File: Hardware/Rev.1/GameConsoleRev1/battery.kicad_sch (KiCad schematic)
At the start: 0 parts

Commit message: Added sprites
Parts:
- added C20: 100n, Capacitor_SMD:C_0402_1005Metric, symbol Device:C
- added D1: BLUE, LED_SMD:LED_0603_1608Metric, symbol Device:LED
- added D2: AMBER, LED_SMD:LED_0603_1608Metric, symbol Device:LED
- added J14: Through Hole, Connector_PinHeader_2.54mm:PinHeader_1x02_P2.54mm_Vertical, symbol Connector:Conn_01x02_Pin
- added J5: JST, Connector_JST:JST_PH_B2B-PH-K_1x02_P2.00mm_Vertical, symbol Connector:Conn_01x02_Pin
- added J6: Pack Temp, Connector_PinHeader_2.54mm:PinHeader_1x02_P2.54mm_Vertical, symbol Connector:Conn_01x02_Pin
- added JP1, JP2, JP3, JP4, JP5: Jumper_2_Open, Jumper:SolderJumper-2_P1.3mm_Open_TrianglePad1.0x1.5mm, symbol Jumper:Jumper_2_Open
- added Q1, Q2: NMOS, Package_TO_SOT_SMD:SOT-23, symbol Transistor_FET:Q_NMOS_GSD
- added R11: 2k2, Resistor_SMD:R_0805_2012Metric, symbol Device:R
- added R12: 330R, Resistor_SMD:R_0805_2012Metric, symbol Device:R
- added R13, R14, R15, R16, R17, R19, R20: 1k, Resistor_SMD:R_0805_2012Metric, symbol Device:R
- added R18: 10k, Resistor_SMD:R_0805_2012Metric, symbol Device:R
- added R21, R22: 10k, Resistor_SMD:R_0402_1005Metric, symbol Device:R
- added R41, R42: 5M1, Resistor_SMD:R_0805_2012Metric, symbol Device:R
- added U2: BQ29700DSER, Package_SON:WSON-6_1.5x1.5mm_P0.5mm, symbol Battery_Management:BQ297xy
- added U3: BQ24073RGT, Package_DFN_QFN:VQFN-16-1EP_3x3mm_P0.5mm_EP1.6x1.6mm, symbol Battery_Management:BQ24073RGT
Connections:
- new net: JP5.1 (A), R22.1
- new net: R16.1, U3.12 (ILIM)
- new net: Q1.1 (G), R41.1, U2.3 (Dout)
- new net: R20.1, U3.4 (~{CE})
- new net: R17.1, U3.14 (TMR)
- new net: JP4.2 (B), R21.1
- new net: D2.1 (K), U3.9 (~{CHG})
- new net: D2.2 (A), R13.2
- new net: C20.1, R12.2, U2.5 (BAT)
- new net: Q2.1 (G), R42.1, U2.2 (Cout)
- new net: Q1.3 (D), Q2.3 (D)
- new net: R19.1, U3.15 (TD)
- new net: R15.1, U3.16 (ISET)
- new net: D1.1 (K), U3.7 (~{PGOOD})
- new net: D1.2 (A), R14.2
- new net: R11.1, U2.6 (V-)
- new net EN1: JP3.2 (B), JP5.2 (B), U3.6 (EN1)
- new net EN2: JP2.1 (A), JP4.1 (A), U3.5 (EN2)
- new net GND: J6.1 (Pin_1), JP1.1 (A), JP2.2 (B), JP3.1 (A), Q2.2 (S), R15.2, R16.2, R17.2, R18.2, R19.2, R20.2, R42.2, U3.17 (VSS), U3.8 (VSS)
- new net IN: U3.13 (IN)
- new net OUT: R13.1, R14.1, R21.2, R22.2, U3.10 (OUT), U3.11 (OUT)
- new net Pack+: J14.2 (Pin_2), J5.1 (Pin_1), R12.1, U3.2 (BAT), U3.3 (BAT)
- new net Pack_UP-: C20.2, J14.1 (Pin_1), J5.2 (Pin_2), JP1.2 (B), Q1.2 (S), R11.2, R41.2, U2.4 (VSS)
- new net TS: J6.2 (Pin_2), R18.1, U3.1 (TS)
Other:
- note added: "10k NTC Thermister"
- note added: "10k Res for no Therm"
- note added: "Set EN1 to 0 and EN2 to OUT for ILIM resisotr charge limit"

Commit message: A
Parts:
- D1: LCSC (none) -> C965804
- D2: LCSC (none) -> C165983
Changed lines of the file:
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@@
+			)
+		)
+		(property "LCSC" "C165983"
+			(at 153.67 71.12 0)
+			(effects
+				(font
+					(size 1.27 1.27)
+				)
 			)
 		)
@@
 			)
 		)
+		(property "LCSC" "C965804"
+			(at 165.1 71.12 0)
+			(effects
+				(font
+					(size 1.27 1.27)
+				)
+			)
+		)

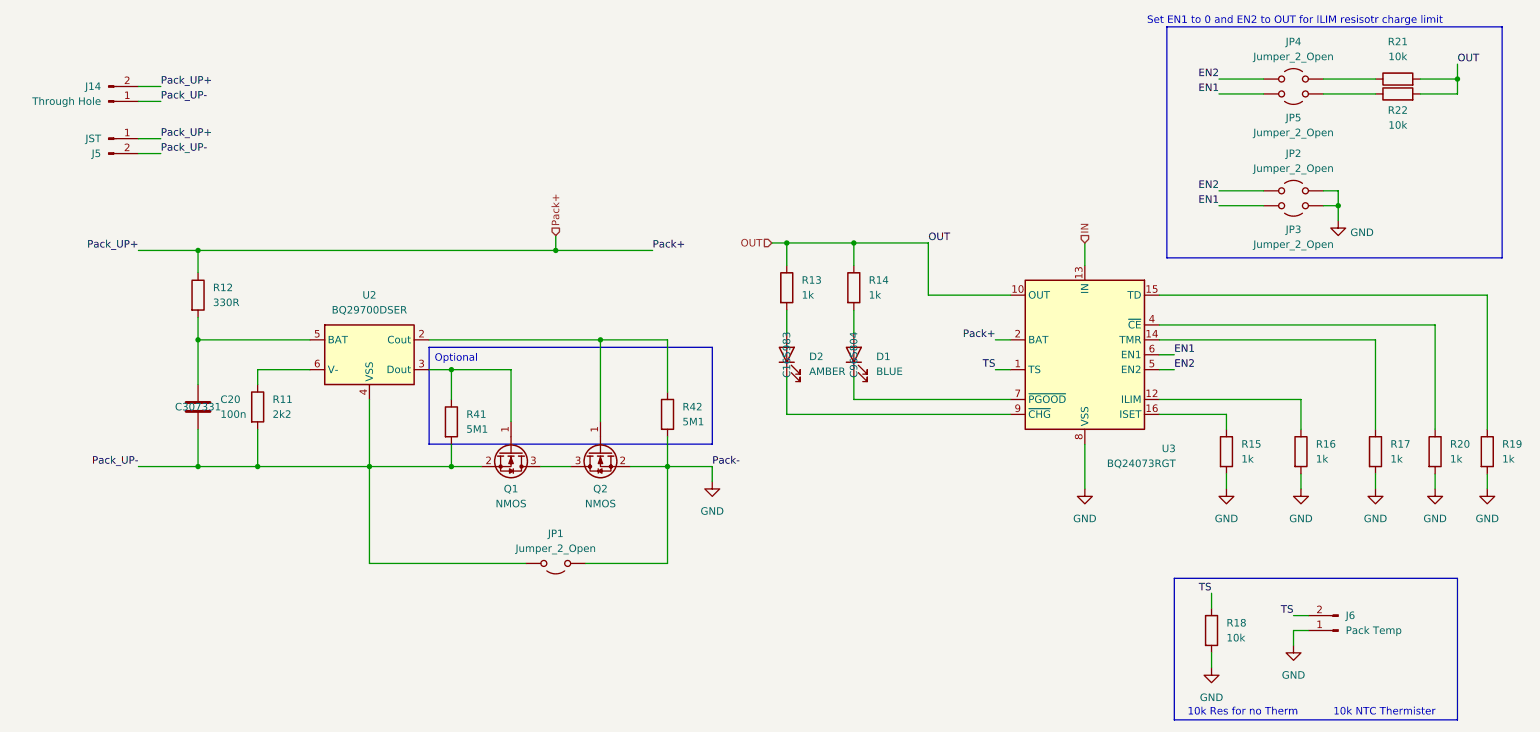
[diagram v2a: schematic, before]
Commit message: Added CPP Build
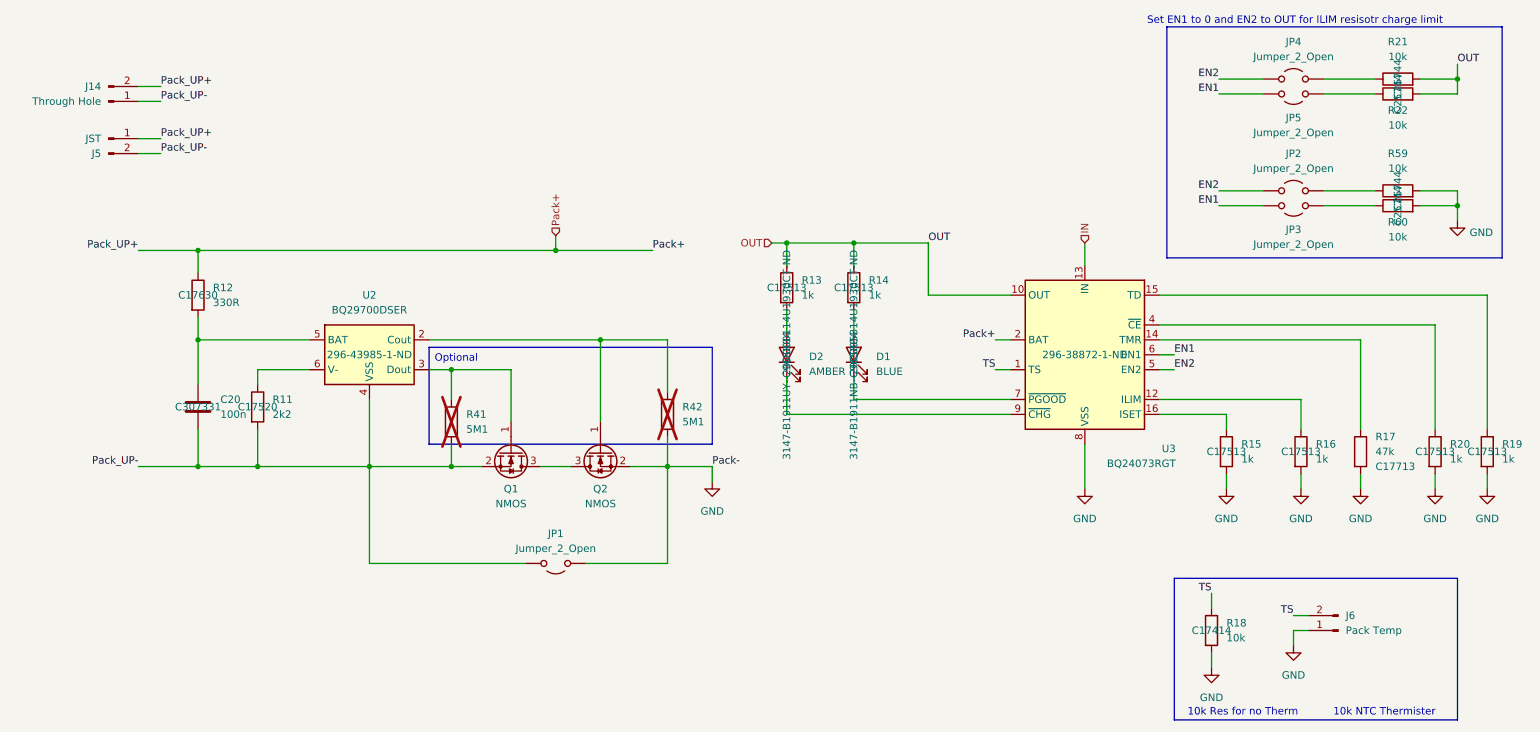
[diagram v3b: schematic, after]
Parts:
- added R59, R60: 10k, Resistor_SMD:R_0402_1005Metric, symbol Device:R
- D1: DK# (none) -> 3147-B1911NB--20C005314U1930CT-ND
- D2: DK# (none) -> 3147-B1911UY--20D000114U1930CT-ND; LCSC C165983 -> C965804
- R11: LCSC (none) -> C17520
- R12: LCSC (none) -> C17630
- R13, R14, R15, R16, R19, R20: LCSC (none) -> C17513
- R17: value 1k -> 47k; LCSC (none) -> C17713
- R18: LCSC (none) -> C17414
- R21, R22: LCSC (none) -> C25744
- R41, R42: now not fitted
- U2: DK# (none) -> 296-43985-1-ND
- U3: DK# (none) -> 296-38872-1-ND
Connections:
- net GND: now also R59.2, R60.2; no longer JP2.2 (B), JP3.1 (A)
- new net: JP3.1 (A), R60.1
- new net: JP2.2 (B), R59.1
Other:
- moved on the sheet: R17
